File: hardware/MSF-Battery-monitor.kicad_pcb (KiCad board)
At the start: 2 copper layers, 106 x 60 mm, 34 parts, among them J1 Chargeur_in, J2 Chargeur_out, J3 USB_B_Mini, J5 PROG, J6 Load_in, J7 Load_out, Q1 BSS138, Q2 IRLML6402, Q3 BSS138, U1 LM358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

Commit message: seconde tentative
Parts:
- added C6: 10u, Capacitor_THT:CP_Radial_D6.3mm_P2.50mm, F.Cu at (114.8, 47.5)
- added C7: 10u, Capacitor_THT:CP_Radial_D6.3mm_P2.50mm, F.Cu at (73.7, 35.3)
- added C8: 10u, Capacitor_THT:CP_Radial_D6.3mm_P2.50mm, F.Cu at (117.5, 55.3)
- added C9: 10u, Capacitor_THT:CP_Radial_D6.3mm_P2.50mm, F.Cu at (59.7, 129.0)
- added R15: 1k, Resistor_THT:R_Axial_DIN0207_L6.3mm_D2.5mm_P10.16mm_Horizontal, F.Cu at (81.0, 83.8)
- added R16: 15k, Resistor_THT:R_Axial_DIN0207_L6.3mm_D2.5mm_P10.16mm_Horizontal, F.Cu at (47.2, 27.9)
- added R18: 5.1k, Resistor_THT:R_Axial_DIN0207_L6.3mm_D2.5mm_P10.16mm_Horizontal, F.Cu at (71.4, 26.9)
- added R19: 1k, Resistor_THT:R_Axial_DIN0207_L6.3mm_D2.5mm_P10.16mm_Horizontal, F.Cu at (77.7, 86.4)
- added R20: 10k, Resistor_THT:R_Axial_DIN0207_L6.3mm_D2.5mm_P10.16mm_Horizontal, F.Cu at (19.1, 84.1)
- added R21: 10k, Resistor_THT:R_Axial_DIN0207_L6.3mm_D2.5mm_P10.16mm_Horizontal, F.Cu at (14.5, 108.5)
- added U5: MCP9700AT-ELT, Package_TO_SOT_SMD:SOT-353_SC-70-5, F.Cu at (101.9, 80.5)
- moved R8 1.52 mm to (70.9, 118.1)
- moved R10 1.52 mm to (60.7, 114.3)
- moved U1 1.44 mm to (64.6, 95.2)
- moved R1 1.44 mm to (72.2, 69.8)
- moved R2 1.44 mm to (72.2, 66.0)
- moved R6 1.27 mm to (71.1, 106.7)
- moved R7 1.27 mm to (71.1, 102.9)
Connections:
- U2 pad 2: Net-(R5-Pad1) -> Net-(U2-Pad2)
- U2 pad 26: unconnected-(U2-Pad26) -> /temperature
- U2 pad 3: Net-(R10-Pad1) -> Net-(U2-Pad3)
- U2 pad 6: unconnected-(U2-Pad6) -> /Chargeur_Vin
- U2 pad 7: unconnected-(U2-Pad7) -> /Load_Vin
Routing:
- net Net-(U2-Pad3): track 0.00 -> 7.37 mm
- net Net-(R10-Pad1): track 44.6 -> 37.7 mm
- net Net-(U2-Pad2): track 0.00 -> 4.06 mm
- net Net-(R5-Pad1): track 37.6 -> 33.8 mm
- net /Load_GND: track 13.5 -> 12.0 mm
- net Net-(J7-Pad1): track 13.5 -> 12.3 mm

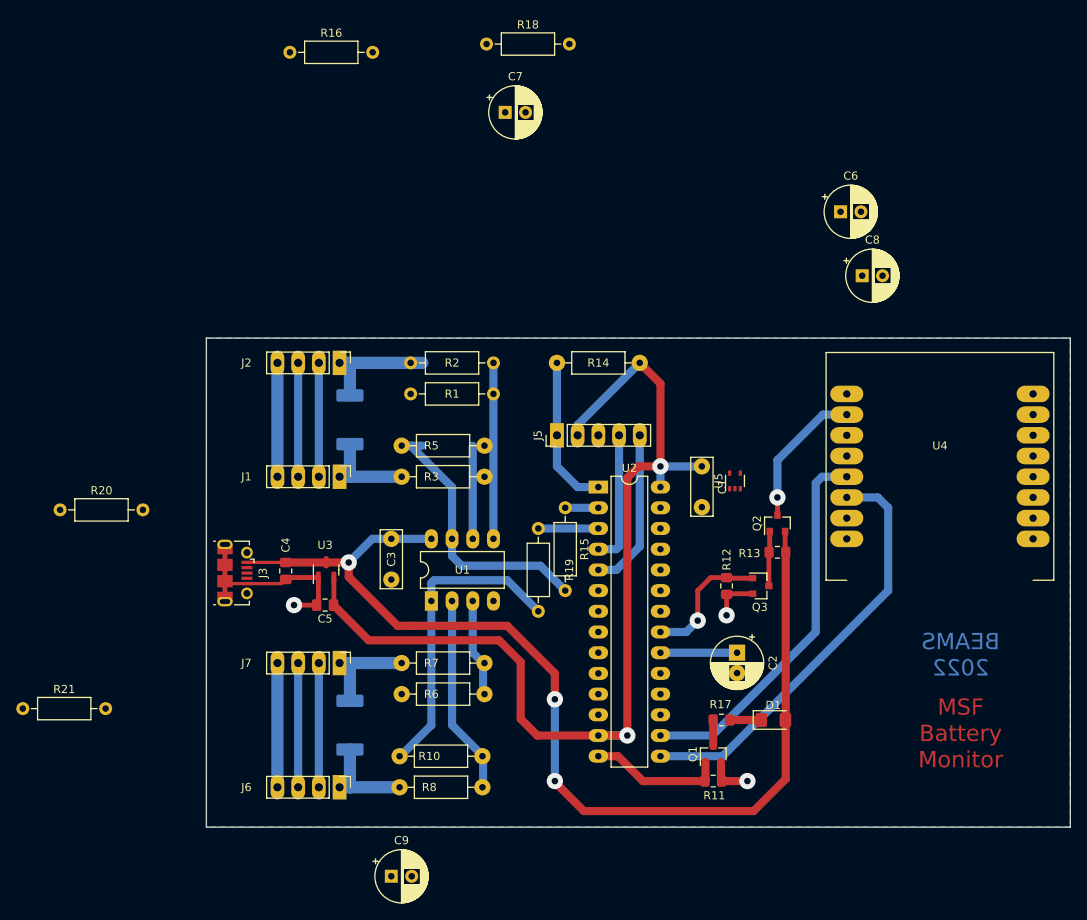
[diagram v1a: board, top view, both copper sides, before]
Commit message: passage au timer1 et mise à jour du PCB
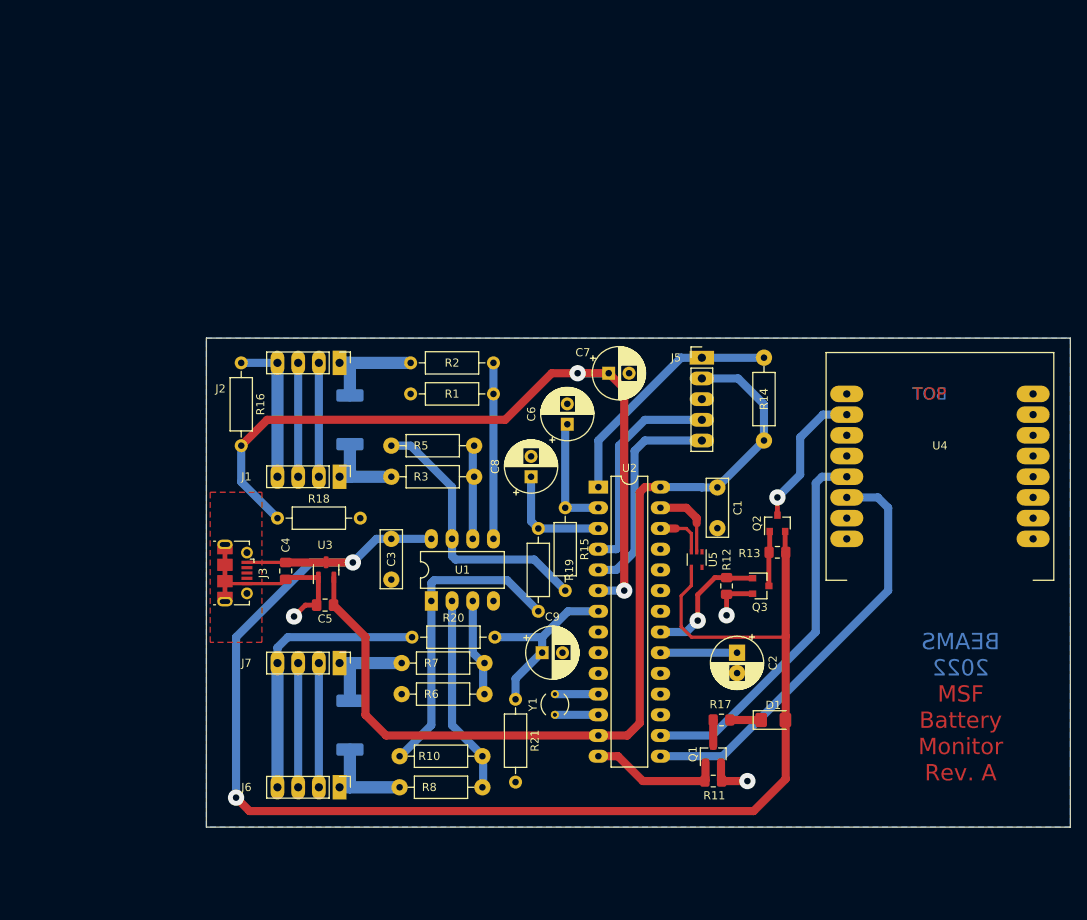
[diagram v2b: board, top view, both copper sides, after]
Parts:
- added Y1: Crystal, Crystal:Crystal_AT310_D3.0mm_L10.0mm_Vertical, F.Cu at (79.8, 109.2)
- moved R18 63.6 mm to (45.7, 85.1)
- moved R21 60.5 mm to (74.9, 107.3), turned to -90 degrees
- moved C8 47.5 mm to (76.8, 80.0), turned to 90 degrees
- moved R20 45.9 mm to (62.2, 99.7)
- moved C6 42.5 mm to (81.3, 73.6), turned to 90 degrees
- moved R16 38.6 mm to (41.3, 66.0), turned to -90 degrees
- moved C7 34.4 mm to (86.4, 67.3)
- moved C9 33.1 mm to (78.2, 101.6)
- moved J5 20.2 mm to (97.8, 65.4), turned to 0 degrees
- moved R14 18.0 mm to (105.4, 75.6), turned to 90 degrees
- moved U5 10.7 mm to (97.2, 90.2), turned to -90 degrees
- moved C1 3.21 mm to (99.7, 81.3)
- moved R3 1.27 mm to (69.8, 80.0)
- moved R5 1.27 mm to (59.7, 76.2)
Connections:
- U2 pad 11: unconnected-(U2-Pad11) -> /SOSCI
- U2 pad 12: unconnected-(U2-Pad12) -> /SOSCO
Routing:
- net /Chargeur_Vin: track 0.00 -> 93.9 mm, vias 0 -> 2
- net +5V: track 131.1 -> 183.0 mm, vias 3 -> 2
- net /Load_Vin: track 0.00 -> 23.0 mm
- net Net-(J6-Pad4): track 15.2 -> 34.2 mm
- net Net-(J5-Pad1): track 18.8 -> 30.2 mm
- net Net-(C6-Pad1): track 4.06 -> 14.6 mm
- net /PGED: track 16.3 -> 26.5 mm
- net +3V3: track 123.4 -> 113.4 mm, vias 2 -> 0
- net GND: track 35.2 -> 44.9 mm
- net Net-(C8-Pad1): track 7.37 -> 14.1 mm
- net /PGEC: track 19.9 -> 26.5 mm
- net /temperature: track 0.00 -> 6.29 mm
- net /SOSCO: track 0.00 -> 5.33 mm
- net /SOSCI: track 0.00 -> 5.33 mm
- net Net-(J1-Pad4): track 14.0 -> 18.4 mm
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- added copper zone on F.Cu, net GND
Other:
- board text added: "BOT"
- board text added: "MSF Battery Monitor Rev. A"
- board text added: "TOP"
- board text removed: "MSF Battery Monitor"
